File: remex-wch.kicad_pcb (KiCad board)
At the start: 4 copper layers, 83.8 x 22.9 mm, 99 parts, among them J1 Conn_01x16, J2 Conn_01x12, J3 USB_C_Receptacle_USB2.0_16P, J4 Micro_SD_Card_Det1, J5 RJ45_Hanrun_HR911130C, J7 JST_PH, SW1 RESET, U1 CH32V307WCU6, U2 RTL8211F, U3 MS5351M, U4 HUSB311, U5 SY6820, U6 LW52xxN11E, U7 LGS5500, U8 PY32F002AW15U, Y1 32.768kHz 12.5 pF Q13FC135000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, Y2 25 MHz 10 pF X322525MMB4SI

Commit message: fix some part values
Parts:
- J4: value Micro_SD_Card_Det1 -> uSD SHOU HAN
- U6: value LW52xxN11E -> LW5233N11E

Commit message: silk, debug, misc
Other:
- board text added: "1"
- board text added: "2"
- board text added: "2024 XXYY"
- board text added: "3"
- board text added: "4"
- board text added: "remex by @ArcaneNibble"
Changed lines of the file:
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@@
 		(layer "F.Fab")
 	)
+	(gr_text "1"
+		(at 126.3 140.2 -90)
+		(layer "F.Cu")
+		(effects
+			(font
+				(size 1 1)
+				(thickness 0.2)
+				(bold yes)
+			)
+			(justify left bottom)
+		)
+	)
+	(gr_text "2"
+		(at 126.3 141.6 270)
+		(layer "In1.Cu")
+		(effects
+			(font
+				(size 1 1)
+				(thickness 0.2)
+				(bold yes)
+			)
+			(justify left bottom)
+		)
+	)
+	(gr_text "3"
+		(at 126.3 143 270)
+		(layer "In2.Cu")
+		(effects
+			(font
+				(size 1 1)
+				(thickness 0.2)
+				(bold yes)
+			)
+			(justify left bottom)
+		)
+	)
+	(gr_text "4"
+		(at 126.3 144.4 270)
+		(layer "B.Cu")
+		(effects
+			(font
+				(size 1 1)
+				(thickness 0.2)
+				(bold yes)
+			)
+			(justify left bottom)
+		)
+	)
+	(gr_text "2024\nXXYY"
+		(at 125.8 143.4 0)
+		(layer "B.Cu")
+		(effects
+			(font
+				(size 1 1)
+				(thickness 0.2)
+				(bold yes)
+			)
+			(justify left bottom mirror)
+		)
+	)
+	(gr_text "remex by\n@ArcaneNibble"
+		(at 100 136 0)
+		(layer "B.SilkS")
+		(effects
+			(font
+				(size 1.5 1.5)
+				(thickness 0.16)
+			)
+			(justify bottom mirror)
+		)
+	)
 	(segment
 		(start 88.98 147.83)
@@
 			)
 		)
+	)
+	(zone
+		(net 0)
+		(net_name "")
+		(layers "F.Cu" "In1.Cu" "In2.Cu" "B.Cu")
+		(name "layerdbg")
+		(hatch edge 0.5)
+		(connect_pads yes
+			(clearance 0)
+		)
+		(min_thickness 0.125)
+		(filled_areas_thickness no)
+		(keepout
+			(tracks allowed)
+			(vias allowed)
+			(pads allowed)
+			(copperpour not_allowed)
+			(footprints allowed)
+		)
+		(fill
+			(thermal_gap 0.5)
+			(thermal_bridge_width 0.5)
+		)
+		(polygon
+			(pts
+				(xy 127.9 139.9) (xy 125.8 139.9) (xy 125.8 146) (xy 127.9 146)
+			)
+		)

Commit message: silk art
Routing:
- net GND: track 96.8 -> 100.9 mm
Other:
- board text added: "CLK2"
- board text added: "NTC"
- board text added: "PC13 TAMPER"
- board text added: "PY32_SWC"
- board text added: "PY32_SWD"
- board text added: "SWC"
- board text added: "SWD"
- board text added: "VBAT"

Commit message: simple trace nudging
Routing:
- net +3.3V: track 218.5 -> 222.9 mm
- net /I2S_MCK: track 16.9 -> 17.5 mm

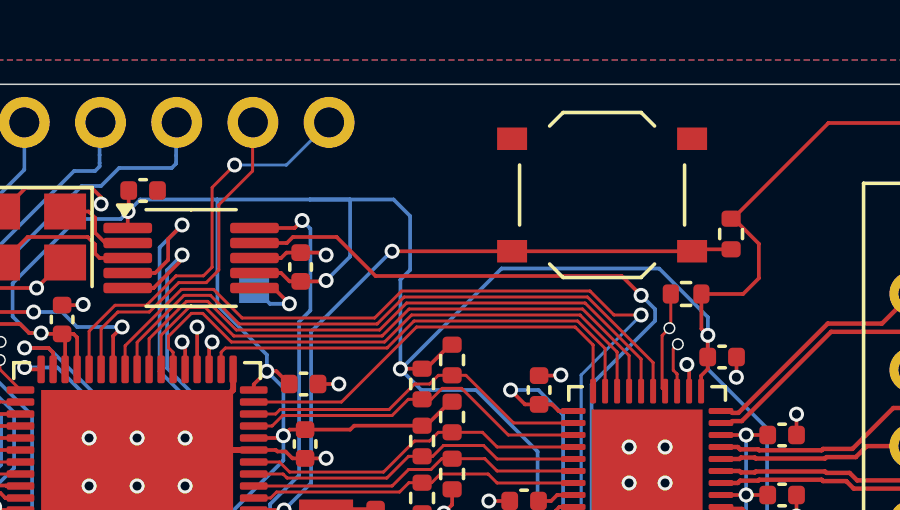
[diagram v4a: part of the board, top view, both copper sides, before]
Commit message: add resest label on top silk
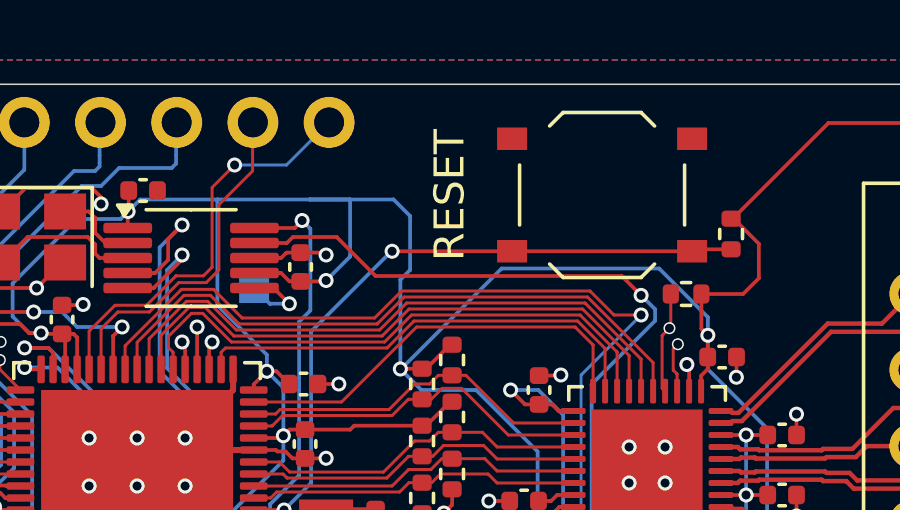
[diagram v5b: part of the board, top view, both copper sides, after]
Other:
- board text added: "RESET"
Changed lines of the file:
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@@
+		)
+	)
+	(gr_text "RESET"
+		(at 93.5 134.5 90)
+		(layer "F.SilkS")
+		(effects
+			(font
+				(size 1 1)
+				(thickness 0.16)
+			)
+			(justify bottom)
 		)
 	)

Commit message: misc poke
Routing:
- net GND: track 100.9 -> 105.8 mm, vias 65 -> 69
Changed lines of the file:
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@@
 	)
 	(segment
-		(start 92.715 145.11)
-		(end 92.725 145.1)
-		(width 0.125)
-		(layer "F.Cu")
-		(net 2)
-	)
-	(segment
 		(start 69.2 134.1)
 		(end 70.1 134.1)
@@
 	)
 	(segment
+		(start 92.725 145.1)
+		(end 92.8 145.1)
+		(width 0.125)
+		(layer "F.Cu")
+		(net 2)
+	)
+	(segment
+		(start 83.9 133.6)
+		(end 83.85 133.55)
+		(width 0.125)
+		(layer "F.Cu")
+		(net 2)
+	)
+	(segment
 		(start 73.1125 138.15)
 		(end 71.85 138.15)
@@
 	)
 	(segment
+		(start 81.05 134)
+		(end 81.3 134.25)
+		(width 0.125)
+		(layer "F.Cu")
+		(net 2)
+	)
+	(segment
 		(start 88.53 140.8)
 		(end 89.225 140.8)
@@
 	)
 	(segment
+		(start 78.95 134)
+		(end 81.05 134)
+		(width 0.125)
+		(layer "F.Cu")
+		(net 2)
+	)
+	(segment
 		(start 50.416 139.04)
 		(end 50.416 138.495)
@@
 	)
 	(segment
+		(start 92.15 146)
+		(end 92 145.85)
+		(width 0.125)
+		(layer "F.Cu")
+		(net 2)
+	)
+	(segment
+		(start 55.3 144.75)
+		(end 55.5 144.95)
+		(width 0.125)
+		(layer "F.Cu")
+		(net 2)
+	)
+	(segment
 		(start 62.825 149.275)
 		(end 62.5 149.6)
@@
 	)
 	(segment
-		(start 88.53 148.9)
-		(end 89.2 148.9)
+		(start 92 145.85)
+		(end 92 145.11)
 		(width 0.125)
 		(layer "F.Cu")
@@
 	)
 	(segment
-		(start 78 135.05)
-		(end 78.7875 134.2625)
+		(start 88.53 148.9)
+		(end 89.2 148.9)
 		(width 0.125)
 		(layer "F.Cu")
@@
 	)
 	(segment
+		(start 83.85 133.55)
+		(end 83.3 133.55)
+		(width 0.125)
+		(layer "F.Cu")
+		(net 2)
+	)
+	(segment
 		(start 101.65 148.11)
 		(end 101.65 148.775)
@@
 	)
 	(segment
+		(start 83.3 133.55)
+		(end 83.15 133.4)
+		(width 0.125)
+		(layer "F.Cu")
+		(net 2)
+	)
+	(segment
 		(start 72.58 134.82)
 		(end 72.6 134.8)
@@
 	)
 	(segment
+		(start 72.1 134)
+		(end 72.4 134)
+		(width 0.125)
+		(layer "F.Cu")
+		(net 2)
+	)
+	(segment
+		(start 92.45 146)
+		(end 92.15 146)
+		(width 0.125)
+		(layer "F.Cu")
+		(net 2)
+	)
+	(segment
+		(start 92.95 145.5)
+		(end 92.45 146)
+		(width 0.125)
+		(layer "F.Cu")
+		(net 2)
+	)
+	(segment
 		(start 58.99 149.09)
 		(end 59.6 149.09)
@@
 	)
 	(segment
+		(start 81.3 134.25)
+		(end 81.3 134.8)
+		(width 0.125)
+		(layer "F.Cu")
+		(net 2)
+	)
+	(segment
 		(start 78.6125 146.6)
 		(end 77.52 146.6)
@@
 	)
 	(segment
-		(start 77.9 135.05)
-		(end 78 135.05)
-		(width 0.125)
-		(layer "F.Cu")
-		(net 2)
-	)
-	(segment
 		(start 90.42 146.87)
 		(end 89.95 146.4)
@@
 	)
 	(segment
+		(start 55.5 144.95)
+		(end 55.5 145.35)
+		(width 0.125)
+		(layer "F.Cu")
+		(net 2)
+	)
+	(segment
 		(start 64.175 148.325)
 		(end 63.6 148.9)
@@
 	)
 	(segment
+		(start 92.95 145.25)
+		(end 92.95 145.5)
+		(width 0.125)
+		(layer "F.Cu")
+		(net 2)
+	)
+	(segment
 		(start 76.95 136)
 		(end 76.95 137.4)
@@
 	)
 	(segment
+		(start 77.9 135.05)
+		(end 78.95 134)
+		(width 0.125)
+		(layer "F.Cu")
+		(net 2)
+	)
+	(segment
 		(start 62.65 140.45)
 		(end 62.21 140.01)
@@
 	)
 	(segment
+		(start 72 133.9)
+		(end 72.1 134)
+		(width 0.125)
+		(layer "F.Cu")
+		(net 2)
+	)
+	(segment
+		(start 92.8 145.1)
+		(end 92.95 145.25)
+		(width 0.125)
+		(layer "F.Cu")
+		(net 2)
+	)
+	(segment
 		(start 58.8 148.9)
 		(end 58.99 149.09)
@@
 	)
 	(segment
-		(start 80.9875 134.2625)
-		(end 81.3 134.575)
+		(start 89.4 149.2)
+		(end 89.4 149.4)
 		(width 0.125)
 		(layer "F.Cu")
@@
 	)
 	(segment
+		(start 89.2 148.9)
+		(end 89.4 149.1)
+		(width 0.125)
+		(layer "F.Cu")
+		(net 2)
+	)
+	(segment
 		(start 87.48 136.42)
 		(end 87.95 136.42)
@@
 	)
 	(segment
-		(start 78.7875 134.2625)
-		(end 80.9875 134.2625)
-		(width 0.125)
-		(layer "F.Cu")
-		(net 2)
-	)
-	(segment
-		(start 92 145.11)
-		(end 92.715 145.11)
-		(width 0.125)
-		(layer "F.Cu")
-		(net 2)
-	)
-	(segment
-		(start 81.3 134.575)
-		(end 81.3 134.8)
-		(width 0.125)
-		(layer "F.Cu")
-		(net 2)
-	)
-	(segment
 		(start 69.5 142.08)
 		(end 69.02 142.08)
@@
 	)
 	(segment
+		(start 89.4 149.4)
+		(end 89.25 149.55)
+		(width 0.125)
+		(layer "F.Cu")
+		(net 2)
+	)
+	(segment
+		(start 89.4 149.1)
+		(end 89.4 149.2)
+		(width 0.125)
+		(layer "F.Cu")
+		(net 2)
+	)
+	(segment
 		(start 55.275 144.775)
 		(end 55.3 144.75)
@@
 	)
 	(via
+		(at 104.5 137)
+		(size 0.5)
+		(drill 0.3)
+		(layers "F.Cu" "B.Cu")
+		(free yes)
+		(net 2)
+	)
+	(via
 		(at 96.625 140.5)
 		(size 0.5)
@@
 	)
 	(via
+		(at 75.6 144.1)
+		(size 0.5)
+		(drill 0.3)
+		(layers "F.Cu" "B.Cu")
+		(free yes)
+		(net 2)
+	)
+	(via
 		(at 68.2 139.45)
 		(size 0.5)
@@
 	)
 	(via
+		(at 98 134)
+		(size 0.5)
+		(drill 0.3)
+		(layers "F.Cu" "B.Cu")
+		(free yes)
+		(net 2)
+	)
+	(via
 		(at 63.85 144.55)
 		(size 0.5)
@@
 	)
 	(via
+		(at 113.5 138.5)
+		(size 0.5)
+		(drill 0.3)
+		(layers "F.Cu" "B.Cu")
+		(free yes)
+		(net 2)
+	)
+	(via
 		(at 54.4 148.45)
 		(size 0.5)
@@
 	)
 	(segment
+		(start 70.75 140.75)
+		(end 70.5 140.75)
+		(width 0.125)
+		(layer "F.Cu")
+		(net 9)
+	)
+	(segment
 		(start 54.2 150.9)
 		(end 69.581382 150.9)
@@
 	)
 	(segment
-		(start 70.13 141.12)
-		(end 70.5 140.75)
-		(width 0.125)
-		(layer "F.Cu")
-		(net 9)
-	)
-	(segment
 		(start 96.425 145.05)
 		(end 96.425 145.5)
@@
 	)
 	(segment
-		(start 71.1 140.15)
-		(end 70.5 140.75)
-		(width 0.125)
-		(layer "F.Cu")
-		(net 9)
-	)
-	(segment
 		(start 96.5 144.5)
 		(end 96.3 144.7)
@@
 	)
 	(segment
+		(start 71.1 139.8)
+		(end 70.5 140.4)
+		(width 0.125)
+		(layer "F.Cu")
+		(net 9)
+	)
+	(segment
 		(start 102.355 135.29)
 		(end 105.545 132.1)
@@
 	)
 	(segment
-		(start 71.6 141.51)
-		(end 71.26 141.51)
-		(width 0.125)
-		(layer "F.Cu")
-		(net 9)
-	)
-	(segment
-		(start 69.5 141.12)
-		(end 70.13 141.12)
-		(width 0.125)
-		(layer "F.Cu")
-		(net 9)
-	)
-	(segment
 		(start 74.675 142.5875)
 		(end 74.675 142.275)
@@
 	)
 	(segment
+		(start 71.6 141.51)
+		(end 71.51 141.51)
+		(width 0.125)
+		(layer "F.Cu")
+		(net 9)
+	)
+	(segment
 		(start 88.8 137.35)
 		(end 88.77 137.38)
@@
 	)
 	(segment
-		(start 71.26 141.51)
-		(end 70.5 140.75)
+		(start 71.51 141.51)
+		(end 70.75 140.75)
 		(width 0.125)
 		(layer "F.Cu")
@@
 	)
 	(segment
+		(start 69.5 141.12)
+		(end 69.87 140.75)
+		(width 0.125)
+		(layer "F.Cu")
+		(net 9)
+	)
+	(segment
 		(start 97.0375 144.9)
 		(end 96.575 144.9)
@@
 	)
 	(segment
-		(start 73.76 149.11)
-		(end 73.75 149.1)
+		(start 69.87 140.75)
+		(end 70.5 140.75)
 		(width 0.125)
 		(layer "F.Cu")
@@
 	)
 	(segment
-		(start 71.1 139.4125)
-		(end 71.1 140.15)
+		(start 73.76 149.11)
+		(end 73.75 149.1)
 		(width 0.125)
 		(layer "F.Cu")
@@
 	)
 	(segment
+		(start 70.5 140.4)
+		(end 70.5 140.75)
+		(width 0.125)
+		(layer "F.Cu")
+		(net 9)
+	)
+	(segment
 		(start 101.31 137.8)
 		(end 102.7 137.8)
@@
 		(layer "F.Cu")
 		(net 9)
+	)
+	(segment
+		(start 71.1 139.4125)
+		(end 71.1 139.8)
+		(width 0.125)
+		(layer "F.Cu")
+		(net 9)
